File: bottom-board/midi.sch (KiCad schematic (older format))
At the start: 14 parts, among them P6 AudioJack3, P7 AudioJack3, Q12 2N7002, Q13 2N7002, U11 6N137S

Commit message: add fabrication files bottom board
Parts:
- P6, P7: MPN (none) -> SJ-3523-SMT-TR
- R47: footprint Resistor_SMD:R_0805_2012Metric -> Resistor_SMD:R_0603_1608Metric; MPN ERJ-P06J221V -> RL73N1JR22JTD
- R49, R50: MPN ERJ-P06J221V -> RL73N1JR22JTD
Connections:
- net at D15.1 (K), U11.2: now also R47.2; no longer R47.1
- net at P6.T: now also R47.1; no longer R47.2
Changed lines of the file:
@@
 $EndDescr
-$Comp
-L bottom-board-rescue:R_Small R47
-U 1 1 550EB368
-P 2850 3550
-F 0 "R47" H 2900 3600 50  0000 L CNN
-F 1 "220R" H 2900 3500 50  0000 L CNN
-F 2 "Resistor_SMD:R_0805_2012Metric" H 2850 3550 60  0001 C CNN
-F 3 "" H 2850 3550 60  0000 C CNN
-F 4 "ERJ-P06J221V" H 100 0   50  0001 C CNN "MPN"
-	1    2850 3550
-	0    1    1    0
-$EndComp
 $Comp
 L bottom-board-rescue:R_Small R49
@@
 F 2 "Resistor_SMD:R_0603_1608Metric" H 6500 3350 60  0001 C CNN
 F 3 "" H 6500 3350 60  0000 C CNN
-F 4 "ERJ-P06J221V" H 200 0   50  0001 C CNN "MPN"
+F 4 "RL73N1JR22JTD" H 200 0   50  0001 C CNN "MPN"
 	1    6500 3350
 	-1   0    0    1
@@
 F 2 "Resistor_SMD:R_0603_1608Metric" H 7700 3550 60  0001 C CNN
 F 3 "" H 7700 3550 60  0000 C CNN
-F 4 "ERJ-P06J221V" H 350 0   50  0001 C CNN "MPN"
+F 4 "RL73N1JR22JTD" H 350 0   50  0001 C CNN "MPN"
 	1    7700 3550
 	0    -1   -1   0
@@
 F 2 "Connector_Audio:Jack_3.5mm_CUI_SJ-3523-SMT_Horizontal" H 7050 3750 50  0001 C CNN
 F 3 "~" H 7050 3750 50  0001 C CNN
+F 4 "SJ-3523-SMT-TR" V 7050 3750 50  0001 C CNN "MPN"
 	1    7050 3750
 	0    -1   -1   0
@@
 F 2 "Connector_Audio:Jack_3.5mm_CUI_SJ-3523-SMT_Horizontal" H 2250 3750 50  0001 C CNN
 F 3 "~" H 2250 3750 50  0001 C CNN
+F 4 "SJ-3523-SMT-TR" V 2250 3750 50  0001 C CNN "MPN"
 	1    2250 3750
 	0    -1   -1   0
@@
 Wire Wire Line
 	4150 3750 4050 3750
+$Comp
+L bottom-board-rescue:R_Small R47
+U 1 1 5DFAB84B
+P 2850 3550
+F 0 "R47" H 2900 3600 50  0000 L CNN
+F 1 "220R" H 2900 3500 50  0000 L CNN
+F 2 "Resistor_SMD:R_0603_1608Metric" H 2850 3550 60  0001 C CNN
+F 3 "" H 2850 3550 60  0000 C CNN
+F 4 "RL73N1JR22JTD" H -3450 200 50  0001 C CNN "MPN"
+	1    2850 3550
+	0    -1   -1   0
+$EndComp
 $EndSCHEMATC

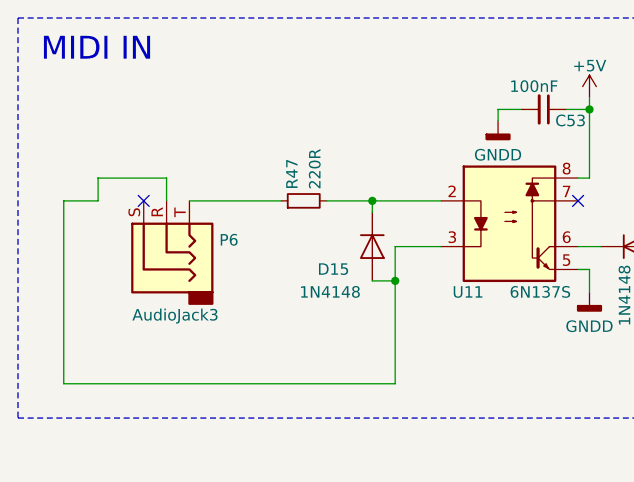
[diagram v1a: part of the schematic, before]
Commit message: change on MIDI input to TRS type A standart + cleanup
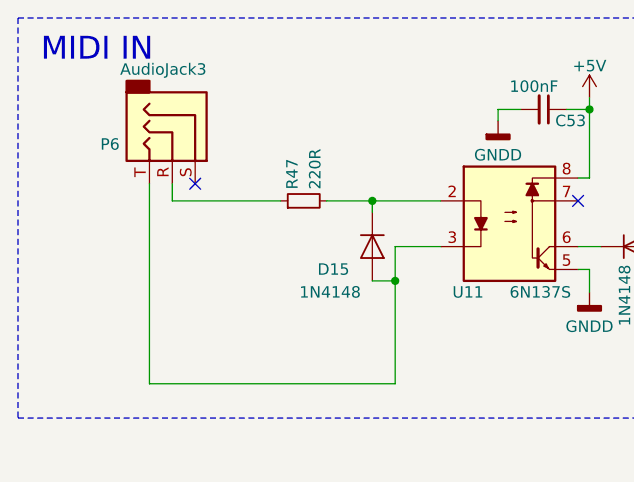
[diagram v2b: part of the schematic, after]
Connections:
- net at D15.2 (A), U11.3: now also P6.T; no longer P6.R
- net at R47.1: now also P6.R; no longer P6.T
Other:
- moved on the sheet: P6
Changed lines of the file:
@@
 Wire Wire Line
 	3250 3750 3450 3750
-Wire Wire Line
-	3250 4350 1800 4350
 Wire Notes Line
 	1600 2750 5450 2750
@@
 Wire Wire Line
 	3700 3150 3700 3200
-Wire Wire Line
-	1800 4350 1800 3550
 Connection ~ 7950 3550
 Connection ~ 8500 3850
@@
 L Connector:AudioJack3 P6
 U 1 1 5D15D509
-P 2250 3750
-F 0 "P6" V 2278 3520 50  0000 R CNN
-F 1 "AudioJack3" V 1950 3900 50  0000 R CNN
-F 2 "Connector_Audio:Jack_3.5mm_CUI_SJ-3523-SMT_Horizontal" H 2250 3750 50  0001 C CNN
-F 3 "~" H 2250 3750 50  0001 C CNN
-F 4 "SJ-3523-SMT-TR" V 2250 3750 50  0001 C CNN "MPN"
-	1    2250 3750
-	0    -1   -1   0
+P 2275 3275
+F 0 "P6" V 2303 3045 50  0000 R CNN
+F 1 "AudioJack3" V 1975 3425 50  0000 R CNN
+F 2 "Connector_Audio:Jack_3.5mm_CUI_SJ-3523-SMT_Horizontal" H 2275 3275 50  0001 C CNN
+F 3 "~" H 2275 3275 50  0001 C CNN
+F 4 "SJ-3523-SMT-TR" V 2275 3275 50  0001 C CNN "MPN"
+	1    2275 3275
+	0    1    1    0
 $EndComp
-Wire Wire Line
-	2350 3550 2750 3550
-Wire Wire Line
-	1950 3550 1950 3450
-Wire Wire Line
-	1950 3450 2250 3450
-Wire Wire Line
-	2250 3450 2250 3550
-Wire Wire Line
-	1800 3550 1950 3550
 Wire Wire Line
 	7150 3550 7600 3550
@@
 Wire Wire Line
 	6950 3500 6950 3550
-NoConn ~ 2150 3550
+NoConn ~ 2375 3475
 $Comp
 L Diode:1N4148 D?
@@
 	0    -1   -1   0
 $EndComp
+Wire Wire Line
+	3250 4350 2175 4350
+Wire Wire Line
+	2175 4350 2175 3475
+Wire Wire Line
+	2750 3550 2275 3550
+Wire Wire Line
+	2275 3550 2275 3475
 $EndSCHEMATC
